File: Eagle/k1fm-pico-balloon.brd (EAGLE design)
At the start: 26.4 x 41.1 mm, 42 parts, among them J1 I2C, J2 ICSP, J3 SERIAL, J4 POWER, Q1 ASTX-H11-25.000MHZ-T, Q2 DMP2305U, Q3 DMP2305U, U1 ATMEGA328, U2 Si5351A-B-GT, U3 MCP1754X-XXXXX/C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

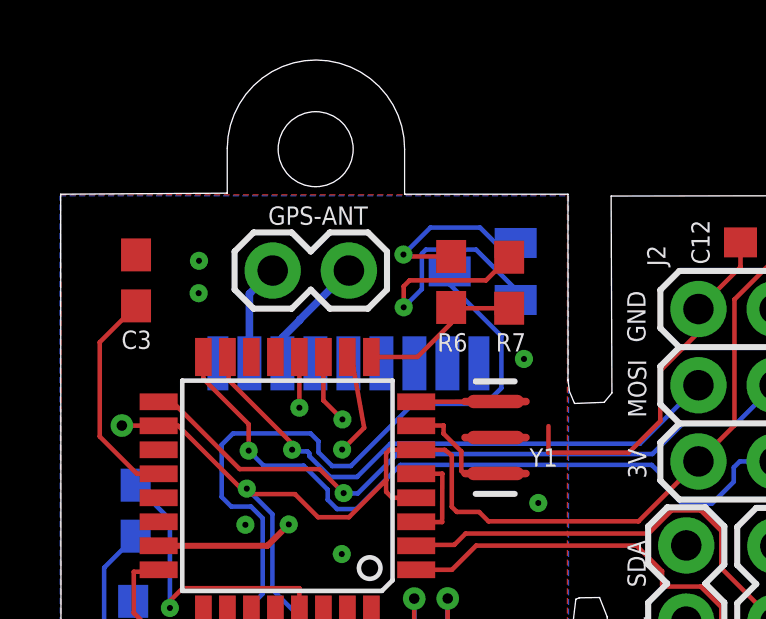
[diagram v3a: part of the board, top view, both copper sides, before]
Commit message: Move board label
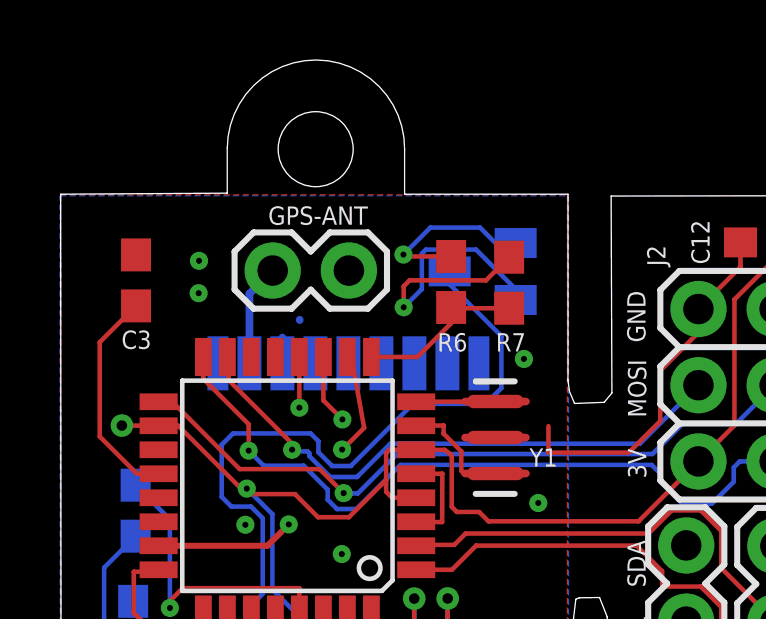
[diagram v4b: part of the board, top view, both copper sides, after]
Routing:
- net GND: track 20.9 -> 17.8 mm
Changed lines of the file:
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@@
 <layers>
 <layer number="1" name="Top" color="4" fill="1" visible="yes" active="yes"/>
-<layer number="2" name="Route2" color="16" fill="1" visible="yes" active="yes"/>
-<layer number="15" name="Route15" color="23" fill="1" visible="yes" active="yes"/>
-<layer number="16" name="Bottom" color="1" fill="1" visible="yes" active="yes"/>
+<layer number="2" name="Route2" color="16" fill="1" visible="no" active="yes"/>
+<layer number="15" name="Route15" color="23" fill="1" visible="no" active="yes"/>
+<layer number="16" name="Bottom" color="1" fill="1" visible="no" active="yes"/>
 <layer number="17" name="Pads" color="2" fill="1" visible="yes" active="yes"/>
 <layer number="18" name="Vias" color="2" fill="1" visible="yes" active="yes"/>
@@
 <layer number="20" name="Dimension" color="24" fill="1" visible="yes" active="yes"/>
 <layer number="21" name="tPlace" color="7" fill="1" visible="yes" active="yes"/>
-<layer number="22" name="bPlace" color="7" fill="1" visible="yes" active="yes"/>
+<layer number="22" name="bPlace" color="7" fill="1" visible="no" active="yes"/>
 <layer number="23" name="tOrigins" color="15" fill="1" visible="yes" active="yes"/>
-<layer number="24" name="bOrigins" color="15" fill="1" visible="yes" active="yes"/>
+<layer number="24" name="bOrigins" color="15" fill="1" visible="no" active="yes"/>
 <layer number="25" name="tNames" color="7" fill="1" visible="yes" active="yes"/>
-<layer number="26" name="bNames" color="7" fill="1" visible="yes" active="yes"/>
+<layer number="26" name="bNames" color="7" fill="1" visible="no" active="yes"/>
 <layer number="27" name="tValues" color="7" fill="1" visible="no" active="yes"/>
 <layer number="28" name="bValues" color="7" fill="1" visible="no" active="yes"/>
@@
 <layer number="38" name="bTest" color="7" fill="1" visible="no" active="yes"/>
 <layer number="39" name="tKeepout" color="4" fill="11" visible="yes" active="yes"/>
-<layer number="40" name="bKeepout" color="1" fill="11" visible="yes" active="yes"/>
+<layer number="40" name="bKeepout" color="1" fill="11" visible="no" active="yes"/>
 <layer number="41" name="tRestrict" color="4" fill="10" visible="yes" active="yes"/>
-<layer number="42" name="bRestrict" color="1" fill="10" visible="yes" active="yes"/>
+<layer number="42" name="bRestrict" color="1" fill="10" visible="no" active="yes"/>
 <layer number="43" name="vRestrict" color="2" fill="10" visible="no" active="yes"/>
 <layer number="44" name="Drills" color="7" fill="1" visible="no" active="yes"/>
@@
 <layer number="50" name="dxf" color="7" fill="1" visible="no" active="no"/>
 <layer number="51" name="tDocu" color="7" fill="1" visible="yes" active="yes"/>
-<layer number="52" name="bDocu" color="7" fill="1" visible="yes" active="yes"/>
+<layer number="52" name="bDocu" color="7" fill="1" visible="no" active="yes"/>
 <layer number="53" name="tGND_GNDA" color="7" fill="9" visible="no" active="no"/>
 <layer number="54" name="bGND_GNDA" color="1" fill="9" visible="no" active="no"/>
@@
 BEFORE
 FLIGHT</text>
-<text x="12.892821875" y="52.08070625" size="1.016" layer="26" rot="MR90">K1FM
+<text x="3.042275" y="78.632575" size="1.016" layer="26" rot="MR270">K1FM
 v 1.3</text>
 <wire x1="4.553053125" y1="80.0339625" x2="4.553053125" y2="81.5339625" width="0" layer="20"/>
@@
 <contactref element="C4" pad="2"/>
 <contactref element="GPS-ANT" pad="1"/>
-<wire x1="8.6076125" y1="77.45479375" x2="6.968553125" y2="75.815734375" width="0.254" layer="16"/>
 <wire x1="6.968553125" y1="75.815734375" x2="6.968553125" y2="75.80084375" width="0.254" layer="16"/>
-<wire x1="6.968553125" y1="75.80084375" x2="6.39139375" y2="75.223684375" width="0.254" layer="16"/>
 <wire x1="6.39139375" y1="75.223684375" x2="6.39139375" y2="74.3614625" width="0.254" layer="16"/>
 <contactref element="U3" pad="1"/>

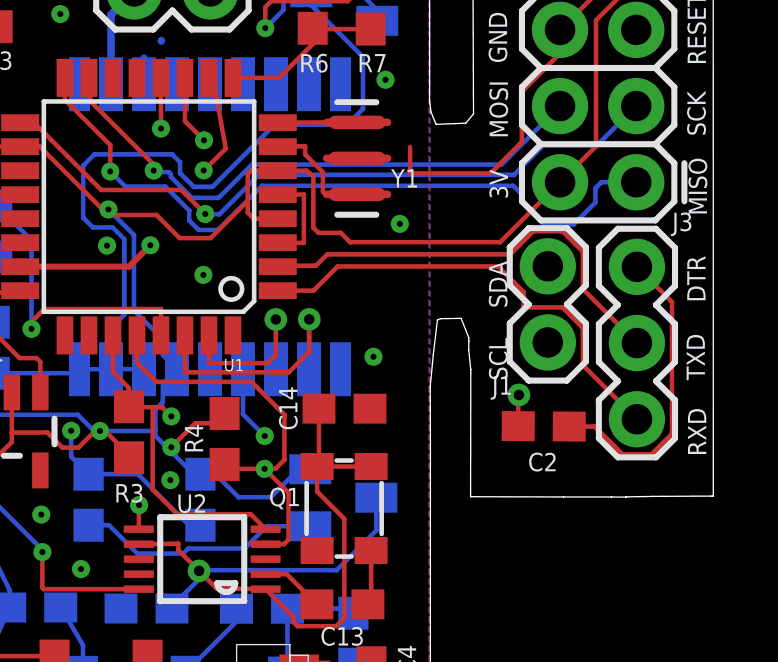
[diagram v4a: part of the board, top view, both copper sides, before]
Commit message: Revert to classic hw/sw serial configuration
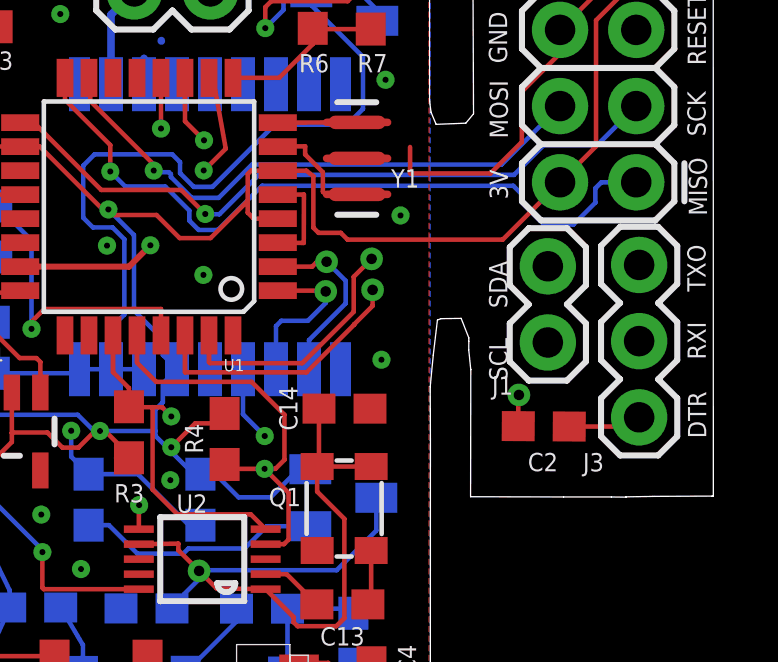
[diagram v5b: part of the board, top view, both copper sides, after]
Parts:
- moved J3 5.02 mm to (22.9, 63.3), turned to 90 degrees
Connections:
- net RXD: now also J3.3; no longer GPS1.2_TXD1
- net RXI: now also GPS1.2_TXD1, U1.2; no longer J3.3, U1.1
- net TXD: now also J3.2; no longer GPS1.3_RXD1
- net TXO: now also GPS1.3_RXD1, U1.1; no longer J3.2, U1.2
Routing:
- net TXD: track 6.09 -> 23.6 mm
- net RXD: track 8.56 -> 19.6 mm
- net RESET: track 44.2 -> 54.1 mm
- net RXI: track 15.4 -> 6.05 mm, vias 0 -> 1
- net TXO: track 14.8 -> 5.41 mm, vias 0 -> 1
- net DTR: track 10.1 -> 2.46 mm
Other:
- board text added: "RXI"
- board text added: "TXO"
- board text removed: "RXD"
- board text removed: "TXD"

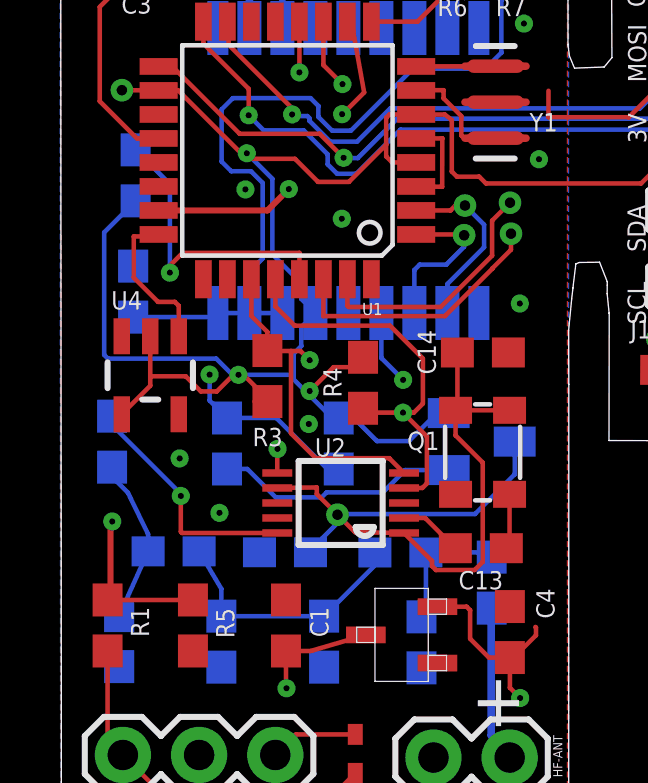
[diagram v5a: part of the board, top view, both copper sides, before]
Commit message: Redraw VDD measure input
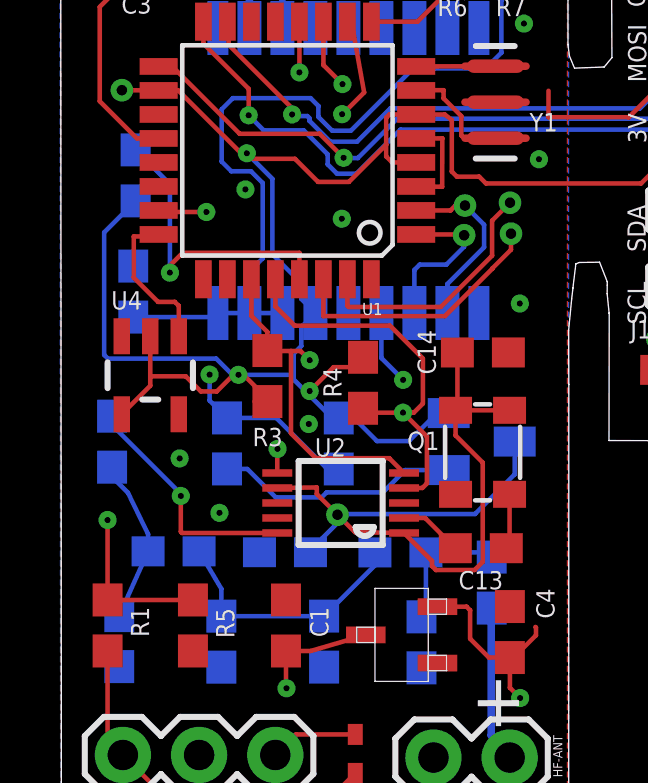
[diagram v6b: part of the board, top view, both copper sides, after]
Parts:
- R1, R5: value 10k -> 4.7k
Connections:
- net N$4 renamed VDD_TST
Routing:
- net VDD_TST: track 24.2 -> 19.2 mm
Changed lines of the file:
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@@
 <attribute name="VALUE" x="0.656003125" y="65.57608125" size="0.6096" layer="28" font="vector" ratio="20" rot="MR90" align="top-center"/>
 </element>
-<element name="R1" library="SparkFun-Resistors" library_urn="urn:adsk.eagle:library:532" package="0603" package3d_urn="urn:adsk.eagle:package:39650/1" value="10k" x="0.56444375" y="54.44650625" smashed="yes" rot="R90">
+<element name="R1" library="SparkFun-Resistors" library_urn="urn:adsk.eagle:library:532" package="0603" package3d_urn="urn:adsk.eagle:package:39650/1" value="4.7k" x="0.56444375" y="54.44650625" smashed="yes" rot="R90">
 <attribute name="NAME" x="1.948071875" y="54.564328125" size="0.6096" layer="25" font="vector" ratio="20" rot="R90" align="bottom-center"/>
 <attribute name="PROD_ID" value="RES-00824" x="0.56444375" y="54.44650625" size="1.27" layer="27" rot="R90" display="off"/>
 <attribute name="VALUE" x="1.32644375" y="54.44650625" size="0.6096" layer="27" font="vector" ratio="20" rot="R90" align="top-center"/>
 </element>
-<element name="R5" library="SparkFun-Resistors" library_urn="urn:adsk.eagle:library:532" package="0603" package3d_urn="urn:adsk.eagle:package:39650/1" value="10k" x="3.40955" y="54.446978125" smashed="yes" rot="R90">
+<element name="R5" library="SparkFun-Resistors" library_urn="urn:adsk.eagle:library:532" package="0603" package3d_urn="urn:adsk.eagle:package:39650/1" value="4.7k" x="3.40955" y="54.446978125" smashed="yes" rot="R90">
 <attribute name="NAME" x="4.78984375" y="54.52568125" size="0.6096" layer="25" font="vector" ratio="20" rot="R90" align="bottom-center"/>
 <attribute name="PROD_ID" value="RES-00824" x="3.40955" y="54.446978125" size="1.27" layer="27" rot="R90" display="off"/>
@@
 <wire x1="5.11453125" y1="48.843815625" x2="8.14895" y2="48.843815625" width="0.1524" layer="1"/>
 </signal>
-<signal name="N$4">
-<contactref element="R1" pad="2"/>
-<contactref element="R5" pad="2"/>
-<contactref element="U1" pad="23"/>
-<wire x1="0.56444375" y1="55.73210625" x2="0.56444375" y2="55.29650625" width="0.1524" layer="1"/>
-<wire x1="0.56444375" y1="55.29650625" x2="3.409078125" y2="55.29650625" width="0.1524" layer="1"/>
-<wire x1="3.409078125" y1="55.29650625" x2="3.40955" y2="55.296978125" width="0.1524" layer="1"/>
-<wire x1="2.265465625" y1="68.28035625" x2="5.891471875" y2="68.28035625" width="0.2032" layer="1"/>
-<wire x1="5.891471875" y1="68.28035625" x2="6.603121875" y2="68.99200625" width="0.2032" layer="1"/>
-<via x="6.603121875" y="68.99200625" extent="1-16" drill="0.2"/>
-<wire x1="6.603121875" y1="68.99200625" x2="2.36938125" y2="64.758265625" width="0.2032" layer="2"/>
-<wire x1="2.36938125" y1="60.23941875" x2="0.66744375" y2="58.53748125" width="0.2032" layer="2"/>
-<wire x1="0.66744375" y1="58.53748125" x2="0.66744375" y2="57.96629375" width="0.2032" layer="2"/>
-<wire x1="0.66744375" y1="57.96629375" x2="0.71960625" y2="57.91413125" width="0.2032" layer="2"/>
-<via x="0.71960625" y="57.91413125" extent="1-16" drill="0.2"/>
-<wire x1="0.71960625" y1="57.91413125" x2="0.661490625" y2="57.856015625" width="0.2032" layer="1"/>
-<wire x1="0.661490625" y1="57.856015625" x2="0.661490625" y2="55.393553125" width="0.2032" layer="1"/>
-<wire x1="0.661490625" y1="55.393553125" x2="0.56444375" y2="55.29650625" width="0.2032" layer="1"/>
-<wire x1="2.36938125" y1="64.758265625" x2="2.36938125" y2="60.23941875" width="0.2032" layer="2"/>
-</signal>
 <signal name="TEMP">
 <contactref element="U4" pad="1"/>
@@
 <wire x1="12.448646875" y1="67.070696875" x2="11.8526375" y2="66.4746875" width="0.1524" layer="16"/>
 </signal>
+<signal name="VDD_TST">
+<contactref element="U1" pad="23"/>
+<contactref element="R5" pad="2"/>
+<contactref element="R1" pad="2"/>
+<wire x1="0.56444375" y1="55.29650625" x2="3.409078125" y2="55.29650625" width="0.1524" layer="1"/>
+<wire x1="3.409078125" y1="55.29650625" x2="3.40955" y2="55.296978125" width="0.1524" layer="1"/>
+<wire x1="0.56444375" y1="55.29650625" x2="0.56444375" y2="57.959628125" width="0.1524" layer="1"/>
+<wire x1="0.56444375" y1="57.959628125" x2="0.56304375" y2="57.961028125" width="0.1524" layer="1"/>
+<via x="0.56304375" y="57.961028125" extent="1-16" drill="0.2"/>
+<wire x1="0.56304375" y1="57.961028125" x2="0.56304375" y2="63.0674375" width="0.1524" layer="2"/>
+<wire x1="0.56304375" y1="63.0674375" x2="4.383309375" y2="66.887703125" width="0.1524" layer="2"/>
+<wire x1="4.383309375" y1="66.887703125" x2="4.383309375" y2="67.702515625" width="0.1524" layer="2"/>
+<wire x1="4.383309375" y1="67.702515625" x2="3.85663125" y2="68.22919375" width="0.1524" layer="2"/>
+<via x="3.85663125" y="68.22919375" extent="1-16" drill="0.2"/>
+<wire x1="3.85663125" y1="68.22919375" x2="2.316628125" y2="68.22919375" width="0.1524" layer="1"/>
+<wire x1="2.316628125" y1="68.22919375" x2="2.265465625" y2="68.28035625" width="0.1524" layer="1"/>
+</signal>
 </signals>

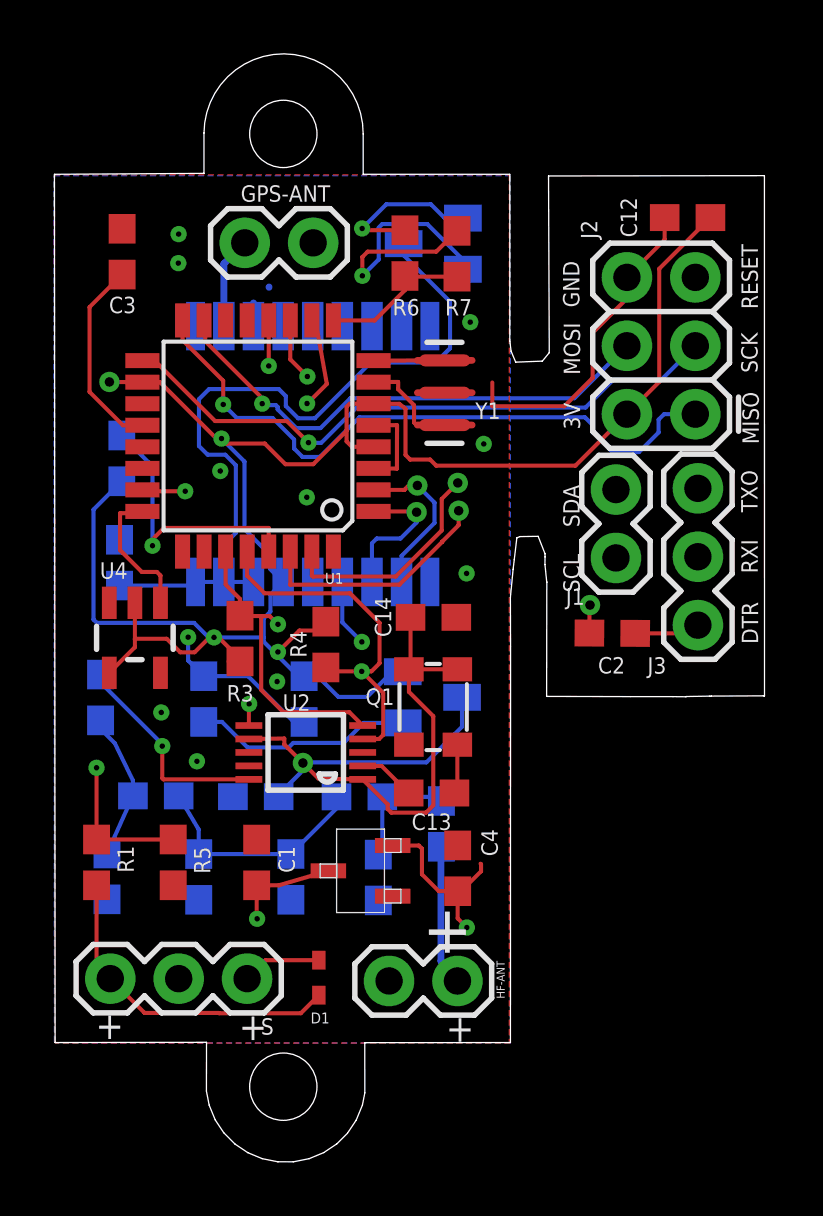
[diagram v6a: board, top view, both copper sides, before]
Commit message: Use diode BAT20J, space out break lines, bugfix
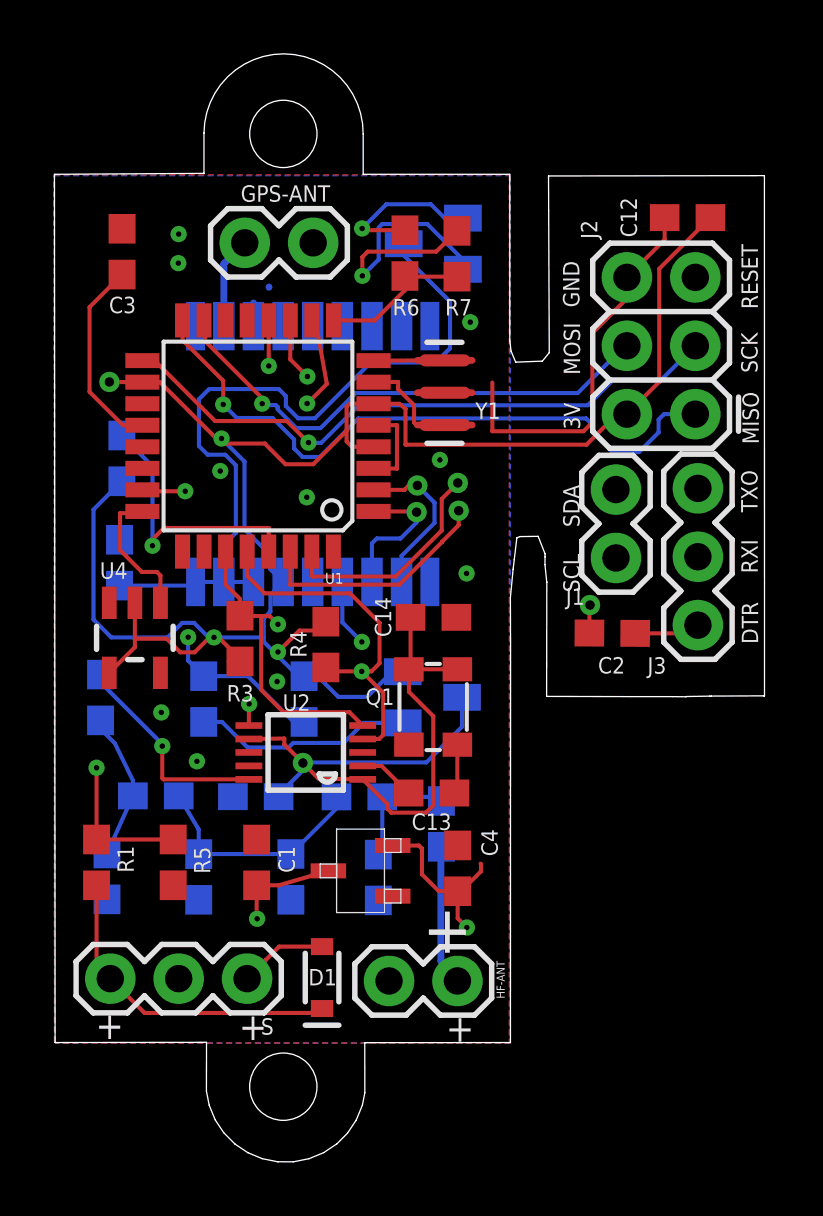
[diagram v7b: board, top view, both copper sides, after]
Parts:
- D1: value 1N4148X-TP -> 1A/23V/620mV; device diode:SOD523 -> SparkFun-DiscreteSemi:SOD-323
- moved D1 0.13 mm to (8.94, 50.2)
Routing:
- net GND: track 17.8 -> 20.1 mm
- net SDA: track 26.3 -> 27.6 mm
- net N$3: track 2.95 -> 4.25 mm
- net RESET: track 54.1 -> 55.1 mm
